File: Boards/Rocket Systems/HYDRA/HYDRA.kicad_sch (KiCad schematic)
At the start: 22 parts, among them IC1 NSVT30010MXV6T1G, IC2 BC846BLT1G, U1 VLMKG3400-GS08

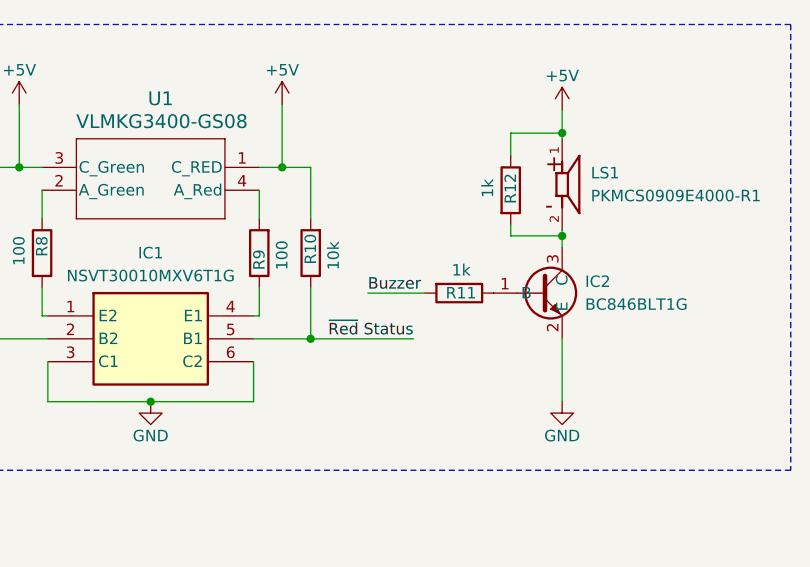
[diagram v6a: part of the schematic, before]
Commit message: ADC sense squematic done
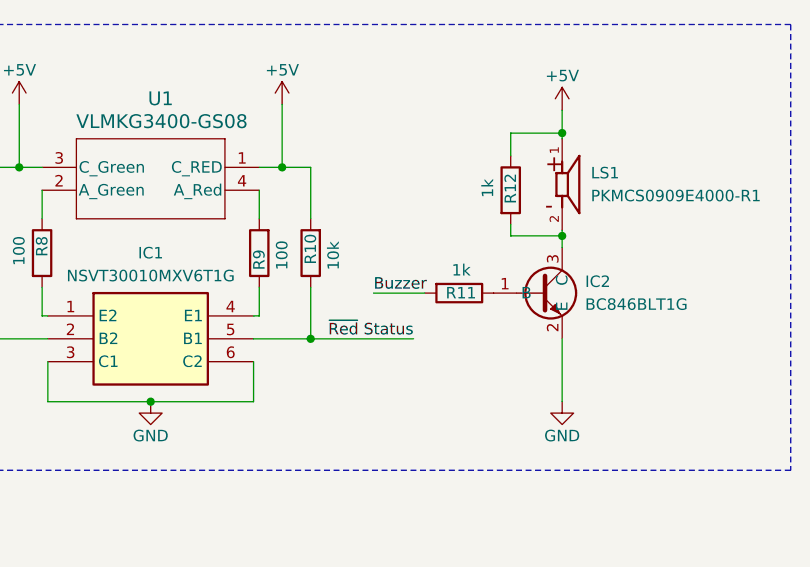
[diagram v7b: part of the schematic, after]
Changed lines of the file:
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@@
 	(wire
 		(pts
-			(xy 207.645 313.69) (xy 213.995 313.69)
+			(xy 208.28 313.69) (xy 213.995 313.69)
 		)
 		(stroke
@@
 		)
 	)
+	(label "Buzzer"
+		(at 208.28 313.69 0)
+		(effects
+			(font
+				(size 1.27 1.27)
+			)
+			(justify left bottom)
+		)
+	)
 	(label "~{Red} Status"
 		(at 235.585 113.03 0)
@@
 		(effects
 			(font
-				(size 1.27 1.27)
-			)
-			(justify left bottom)
-		)
-	)
-	(label "Buzzer"
-		(at 207.645 313.69 0)
-		(effects
-			(font

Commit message: HYDRA Schematic Update Final Touches
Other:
- sheet Actuation Unit ports: added CAM IN, CAM OUT; removed CAM 1 IN, CAM 1 OUT, CAM 2 IN, CAM 2 OUT, CAM 3 IN, CAM 3 OUT
- note added: "TODO: Escolher connectores ADC FAULT DESIGN ATUALIZAR PROJECT SYMBOLS LIB ADICIONAR FOOTPRINTS CORRER ERC -- LAYOUT"
- note removed: "TODO: Escolher connectores Filtros Anti-aliasing ADC FAULT DESIGN ATUALIZAR PROJECT SYMBOLS LIB ADICIONAR FOOTPRINTS CORRER ERC -- LAYOUT"
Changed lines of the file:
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@@
 		)
 	)
-	(text "TODO:\nEscolher connectores\nFiltros Anti-aliasing\nADC FAULT DESIGN\n\nATUALIZAR PROJECT SYMBOLS LIB\nADICIONAR FOOTPRINTS\nCORRER ERC\n-- LAYOUT"
+	(text "TODO:\nEscolher connectores\nADC FAULT DESIGN\n\nATUALIZAR PROJECT SYMBOLS LIB\nADICIONAR FOOTPRINTS\nCORRER ERC\n-- LAYOUT"
 		(exclude_from_sim no)
 		(at 386.08 340.995 0)
@@
 	(wire
 		(pts
-			(xy 140.335 243.84) (xy 165.1 243.84)
-		)
-		(stroke
-			(width 0)
-			(type default)
-		)
-	)
-	(wire
-		(pts
 			(xy 249.555 115.57) (xy 235.585 115.57)
 		)
@@
 	(wire
 		(pts
-			(xy 140.335 252.095) (xy 165.1 252.095)
-		)
-		(stroke
-			(width 0)
-			(type default)
-		)
-	)
-	(wire
-		(pts
 			(xy 139.7 168.275) (xy 165.1 168.275)
 		)
@@
 	(wire
 		(pts
-			(xy 140.335 249.555) (xy 165.1 249.555)
-		)
-		(stroke
-			(width 0)
-			(type default)
-		)
-	)
-	(wire
-		(pts
 			(xy 127 79.375) (xy 165.1 79.375)
 		)
@@
 	(wire
 		(pts
-			(xy 140.335 246.38) (xy 165.1 246.38)
-		)
-		(stroke
-			(width 0)
-			(type default)
-		)
-	)
-	(wire
-		(pts
 			(xy 140.335 224.155) (xy 165.1 224.155)
 		)
@@
 		)
 	)
-	(label "CAM 2 IN"
-		(at 140.335 243.84 0)
-		(effects
-			(font
-				(size 1.27 1.27)
-			)
-			(justify left bottom)
-		)
-	)
 	(label "THERMO2 DN"
 		(at 152.4 52.07 0)
@@
 		)
 	)
-	(label "CAM 2 OUT"
-		(at 140.335 246.38 0)
-		(effects
-			(font
-				(size 1.27 1.27)
-			)
-			(justify left bottom)
-		)
-	)
 	(label "~{CS} THERMO2 SPI"
 		(at 219.075 46.99 0)
@@
 		)
 	)
-	(label "CAM 3 OUT"
-		(at 140.335 252.095 0)
-		(effects
-			(font
-				(size 1.27 1.27)
-			)
-			(justify left bottom)
-		)
-	)
 	(label "MOSI SPI"
 		(at 219.075 57.15 0)
@@
 		)
 	)
-	(label "CAM 3 IN"
-		(at 140.335 249.555 0)
-		(effects
-			(font
-				(size 1.27 1.27)
-			)
-			(justify left bottom)
-		)
-	)
 	(label "MISO SPI"
 		(at 219.075 54.61 0)
@@
 			)
 		)
-		(pin "CAM 1 IN" input
+		(pin "CAM IN" input
 			(at 165.1 238.125 180)
 			(effects
@@
 			)
 		)
-		(pin "CAM 1 OUT" input
+		(pin "CAM OUT" input
 			(at 165.1 240.665 180)
 			(effects
 				(font
-					(size 1.27 1.27)
-				)
-				(justify left)
-			)
-		)
-		(pin "CAM 2 IN" input
-			(at 165.1 243.84 180)
-			(effects
-				(font
-					(size 1.27 1.27)
-				)
-				(justify left)
-			)
-		)
-		(pin "CAM 2 OUT" input
-			(at 165.1 246.38 180)
-			(effects
-				(font
-					(size 1.27 1.27)
-				)
-				(justify left)
-			)
-		)
-		(pin "CAM 3 IN" input
-			(at 165.1 249.555 180)
-			(effects
-				(font
-					(size 1.27 1.27)
-				)
-				(justify left)
-			)
-		)
-		(pin "CAM 3 OUT" input
-			(at 165.1 252.095 180)
-			(effects
-				(font
